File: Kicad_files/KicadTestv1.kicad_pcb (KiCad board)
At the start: 2 copper layers, 18 parts, among them J1 Conn_01x04, J2 Conn_01x04, SW1 SW_Push, U1 RN2483A, U2 LTC1050

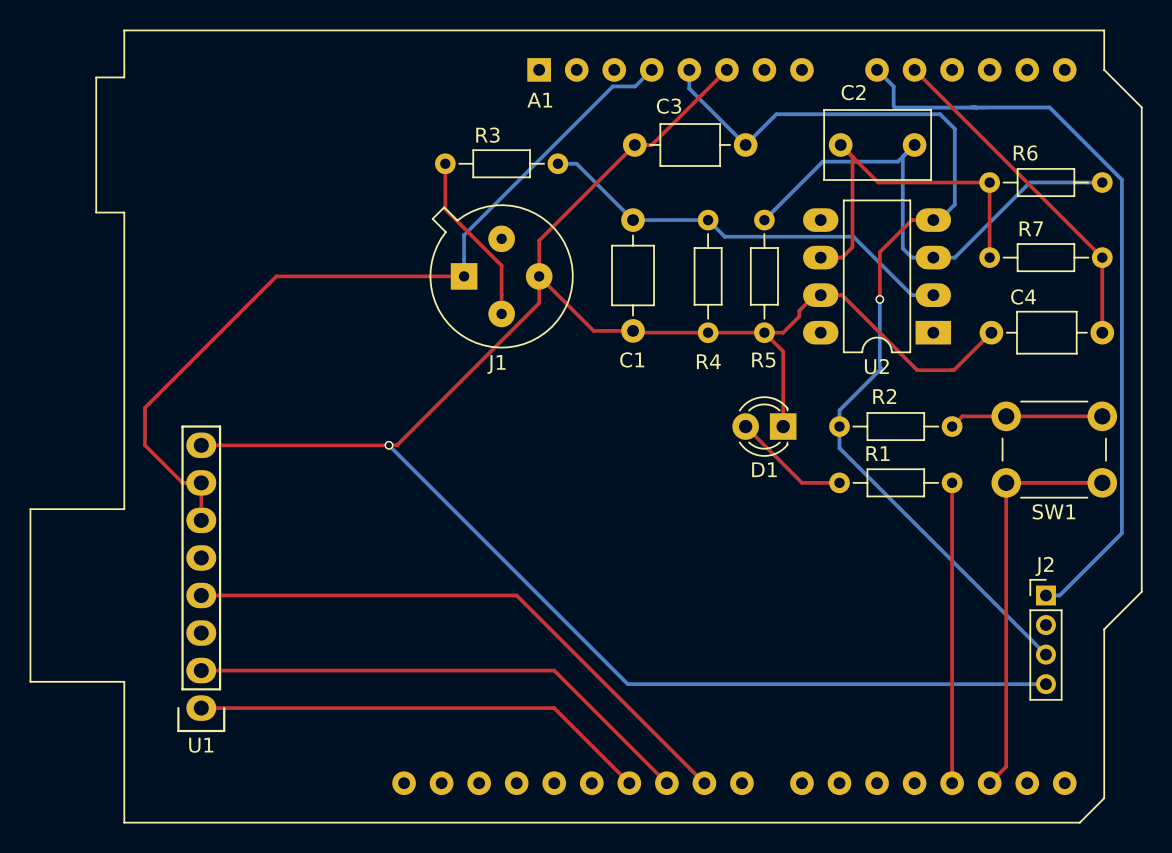
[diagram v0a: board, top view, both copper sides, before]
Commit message: Changement sensor Gaz
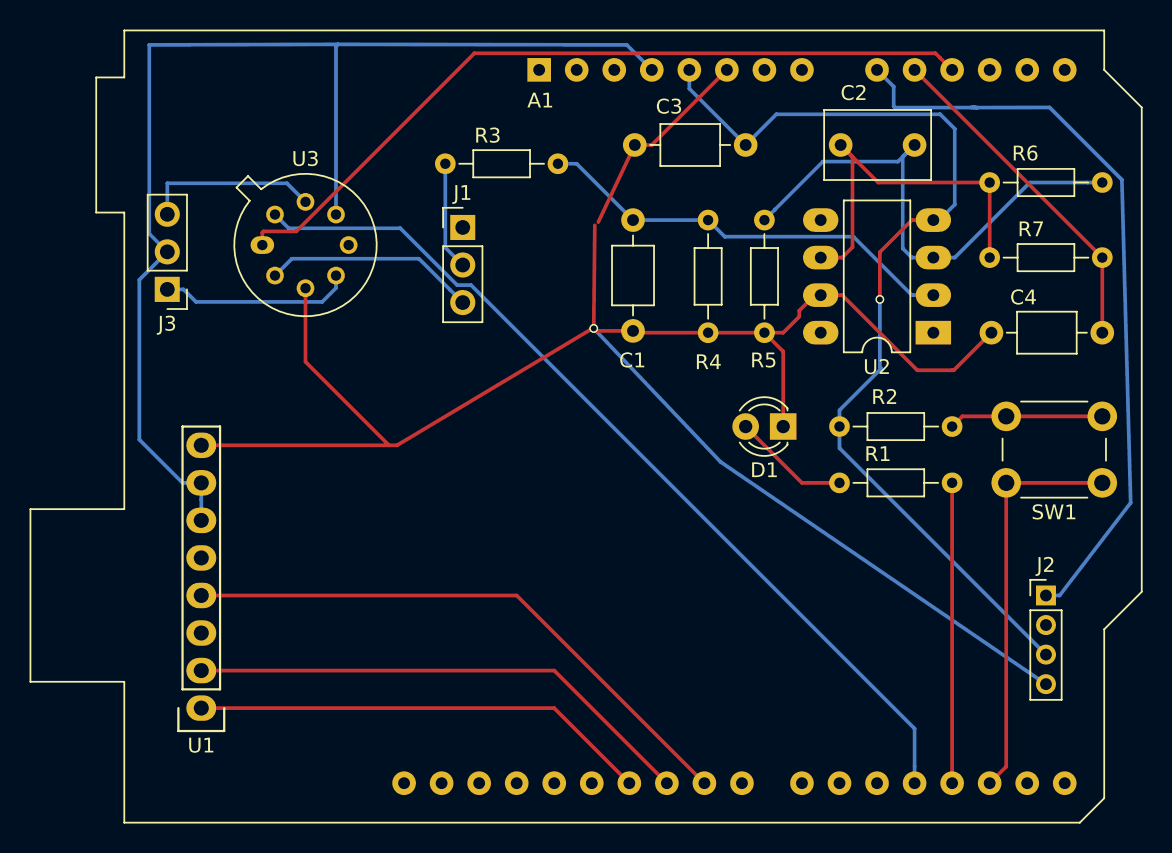
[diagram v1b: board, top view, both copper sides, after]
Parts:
- added J3: Conn_01x03, Connector_PinHeader_2.54mm:PinHeader_1x03_P2.54mm_Vertical, F.Cu at (114.5, 89.8)
- added U3: GazSensor, Package_TO_SOT_THT:TO-5-8, F.Cu at (121.0, 86.8)
- J1: value Conn_01x04 -> Conn_01x03; footprint ShieldArduino_Empreintes:TO-5-4_1 -> Connector_PinHeader_2.54mm:PinHeader_1x03_P2.54mm_Vertical
- moved J1 3.31 mm to (134.5, 85.6)
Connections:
- net Net-(J1-Pad2) renamed Rsensor
- A1 pad 11: Net-(A1-Pad11) -> CapTemp
- A1 pad 19: Net-(A1-Pad19) -> RChauff
- J1 pad 1: +3V3 -> Net-(J1-Pad1)
- J1 pad 3: GND -> Net-(J1-Pad3)
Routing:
- net RChauff: track 0.00 -> 61.4 mm
- net CapTemp: track 0.00 -> 53.1 mm
- net +3V3: track 55.3 -> 82.2 mm
- net Net-(J1-Pad3): track 0.00 -> 14.4 mm
- net Net-(J3-Pad1): track 0.00 -> 13.0 mm
- net Net-(J3-Pad3): track 0.00 -> 12.0 mm
- net Rsensor: track 11.7 -> 7.34 mm
- net GND: track 143.2 -> 140.4 mm

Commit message: Changement nom Schema
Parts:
- J1: value Conn_01x03 -> ReadGas
- J2: value Conn_01x04 -> GrooveGasSensor
- J3: value Conn_01x03 -> Alimentation
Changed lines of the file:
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@@
       (effects (font (size 1 1) (thickness 0.15)))
     )
-    (fp_text value Conn_01x03 (at 0 7.41) (layer F.Fab)
+    (fp_text value Alimentation (at -2.92 -4.42) (layer F.Fab)
       (effects (font (size 1 1) (thickness 0.15)))
     )
@@
       (effects (font (size 1 1) (thickness 0.15)))
     )
-    (fp_text value Conn_01x03 (at 0 7.41) (layer F.Fab)
+    (fp_text value ReadGas (at -0.08 8.68) (layer F.Fab)
       (effects (font (size 1 1) (thickness 0.15)))
     )
@@
       (effects (font (size 1 1) (thickness 0.15)))
     )
-    (fp_text value Conn_01x04 (at 0 8.06) (layer F.Fab)
-      (effects (font (size 1 1) (thickness 0.15)))
-    )
+    (fp_text value GrooveGasSensor (at 2.68 4.89 90) (layer F.Fab)
+      (effects (font (size 1 1) (thickness 0.15)))
+    )
